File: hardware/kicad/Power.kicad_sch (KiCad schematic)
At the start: 53 parts, among them J1 USB_C_Receptacle_USB2.0_16P, Q1 FDN304PZ, SW1 SW_SPDT_321, U1 TPS61023DRLR, U2 MCP73871-2CC, U3 TLV74333PDBVR, U4 TLV74333PDBVR

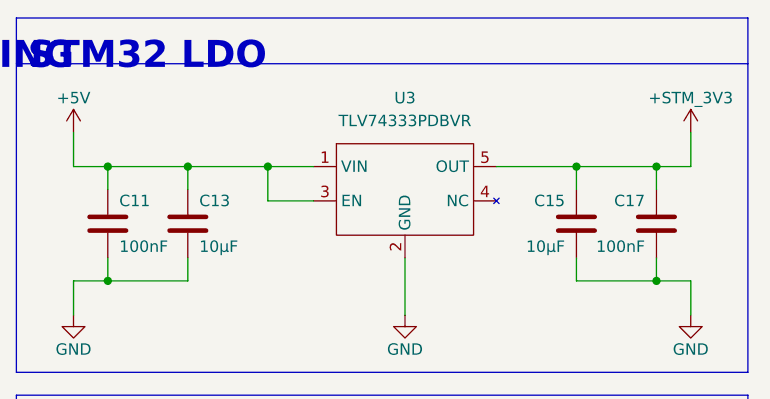
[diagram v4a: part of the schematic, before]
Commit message: completed schematics and started pcb
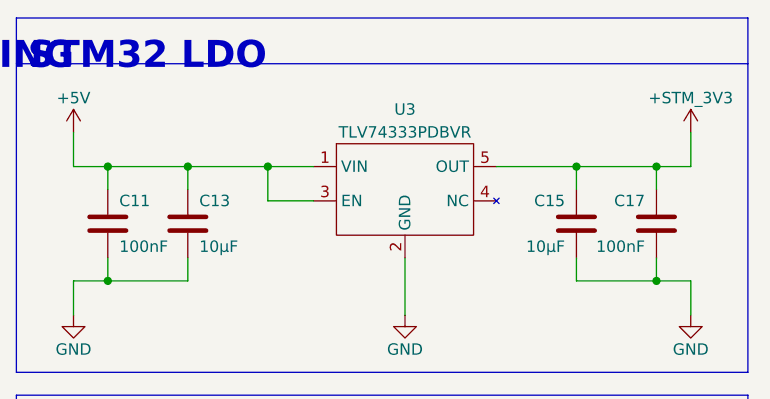
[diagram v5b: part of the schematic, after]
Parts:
- U2: footprint Package_DFN_QFN:QFN-20-1EP_4x4mm_P0.5mm_EP2.5x2.5mm -> Package_DFN_QFN:QFN-20-1EP_4x4mm_P0.5mm_EP2.5x2.5mm_ThermalVias
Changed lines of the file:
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@@
+	)
+	(symbol
+		(lib_id "TLV74333PDBVR:TLV74333PDBVR")
+		(at 245.11 33.02 0)
+		(unit 1)
+		(body_style 1)
+		(exclude_from_sim no)
+		(in_bom yes)
+		(on_board yes)
+		(in_pos_files yes)
+		(dnp no)
+		(property "Reference" "U3"
+			(at 245.11 24.13 0)
+			(show_name no)
+			(do_not_autoplace no)
+			(effects
+				(font
+					(size 1.27 1.27)
+				)
+			)
+		)
+		(property "Value" "TLV74333PDBVR"
+			(at 245.11 26.67 0)
+			(show_name no)
+			(do_not_autoplace no)
+			(effects
+				(font
+					(size 1.27 1.27)
+				)
+			)
+		)
+		(property "Footprint" "Package_TO_SOT_SMD:SOT-23-5_HandSoldering"
+			(at 246.38 52.07 0)
+			(hide yes)
+			(show_name no)
+			(do_not_autoplace no)
+			(effects
+				(font
+					(size 1.27 1.27)
+				)
+			)
+		)
+		(property "Datasheet" ""
+			(at 245.11 33.02 0)
+			(hide yes)
+			(show_name no)
+			(do_not_autoplace no)
+			(effects
+				(font
+					(size 1.27 1.27)
+				)
+			)
+		)
+		(property "Description" ""
+			(at 245.11 33.02 0)
+			(hide yes)
+			(show_name no)
+			(do_not_autoplace no)
+			(effects
+				(font
+					(size 1.27 1.27)
+				)
+			)
+		)
+		(pin "2"
+		)
+		(pin "5"
+		)
+		(pin "4"
+		)
+		(pin "1"
+		)
+		(pin "3"
+		)
+		(instances
+			(project "crypto_node"
+				(path "/6c72b0cb-17b9-42a6-811c-297d0c354af3/0878dbd6-f23a-45b7-803f-70f55a38d748"
+					(reference "U3")
+					(unit 1)
+				)
+			)
+		)
 	)
 	(symbol
@@
 			)
 		)
-		(property "Footprint" "Package_DFN_QFN:QFN-20-1EP_4x4mm_P0.5mm_EP2.5x2.5mm"
+		(property "Footprint" "Package_DFN_QFN:QFN-20-1EP_4x4mm_P0.5mm_EP2.5x2.5mm_ThermalVias"
 			(at 134.62 119.38 0)
 			(hide yes)
@@
 					(unit 1)
 				)
-			)
-		)
-	)
-	(symbol
-		(lib_id "TLV74333PDBVR:TLV74333PDBVR")
-		(at 245.11 33.02 0)
-		(unit 1)
-		(body_style 1)
-		(exclude_from_sim no)
-		(in_bom yes)
-		(on_board yes)
-		(in_pos_files yes)
-		(dnp no)
-		(fields_autoplaced yes)
-		(property "Reference" "U3"
-			(at 245.11 22.86 0)
-			(show_name no)
-			(do_not_autoplace no)
-			(effects
-				(font
-					(size 1.27 1.27)
-				)
-			)
-		)
-		(property "Value" "TLV74333PDBVR"
-			(at 245.11 25.4 0)
-			(show_name no)
-			(do_not_autoplace no)
-			(effects
-				(font
-					(size 1.27 1.27)
-				)
-			)
-		)
-		(property "Footprint" "Package_TO_SOT_SMD:SOT-23-5_HandSoldering"
-			(at 246.38 52.07 0)
-			(hide yes)
-			(show_name no)
-			(do_not_autoplace no)
-			(effects
-				(font
-					(size 1.27 1.27)
-				)
-			)
-		)
-		(property "Datasheet" ""
-			(at 245.11 33.02 0)
-			(hide yes)
-			(show_name no)
-			(do_not_autoplace no)
-			(effects
-				(font
-					(size 1.27 1.27)
-				)
-			)
-		)
-		(property "Description" ""
-			(at 245.11 33.02 0)
-			(hide yes)
-			(show_name no)
-			(do_not_autoplace no)
-			(effects
-				(font
-					(size 1.27 1.27)
-				)
-			)
-		)
-		(pin "2"
-		)
-		(pin "5"
-		)
-		(pin "4"
-		)
-		(pin "1"
-		)
-		(pin "3"
-		)
-		(instances
-			(project "crypto_node"
-				(path "/6c72b0cb-17b9-42a6-811c-297d0c354af3/0878dbd6-f23a-45b7-803f-70f55a38d748"
-					(reference "U3")
-					(unit 1)
-				)

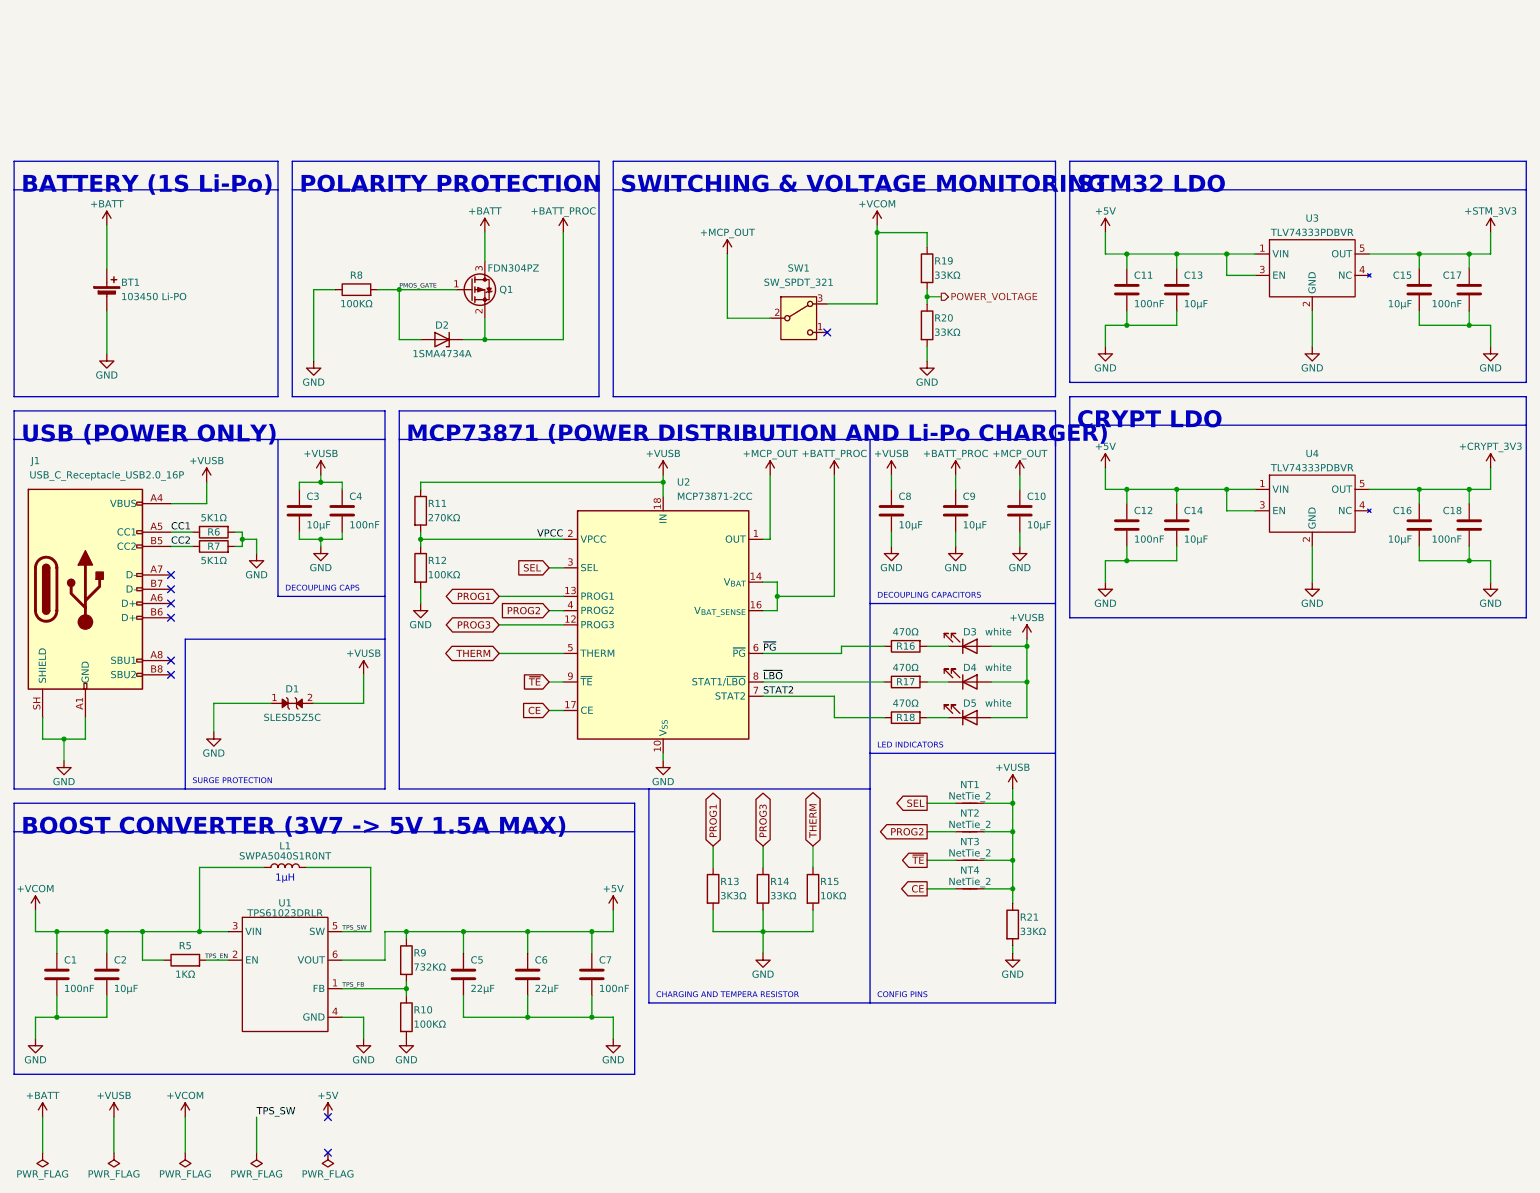
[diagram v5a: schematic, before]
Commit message: started PCB and changed power system
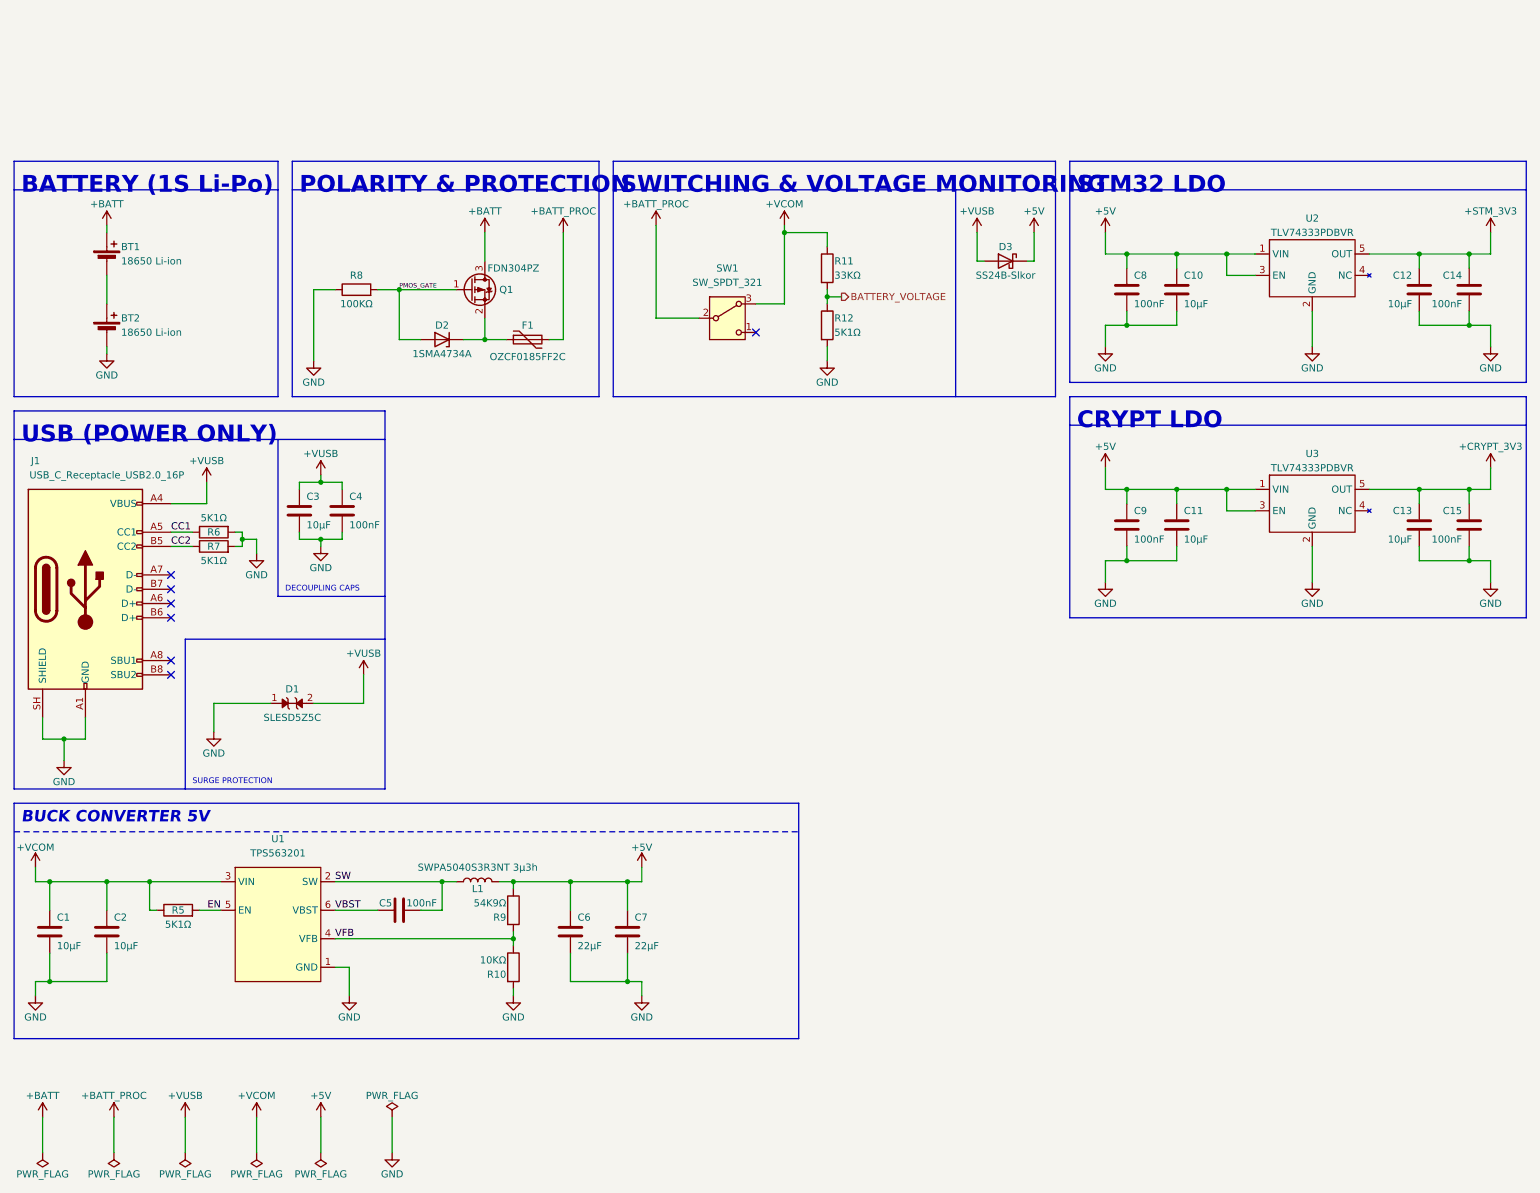
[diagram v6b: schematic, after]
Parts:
- removed C10, C8, C9: 10μF, Capacitor_SMD:C_1206_3216Metric_Pad1.33x1.80mm_HandSolder, symbol Device:C
- removed D3, D4, D5: white, LED_SMD:LED_0805_2012Metric_Pad1.15x1.40mm_HandSolder, symbol Device:LED
- removed NT1, NT2, NT3, NT4: NetTie_2, NetTie:NetTie-2_SMD_Pad0.5mm, symbol Device:NetTie_2
- removed R11: 270KΩ, Resistor_SMD:R_0805_2012Metric_Pad1.20x1.40mm_HandSolder, symbol Device:R
- removed R13: 3K3Ω, Resistor_SMD:R_0805_2012Metric_Pad1.20x1.40mm_HandSolder, symbol Device:R
- removed R14, R20, R21: 33KΩ, Resistor_SMD:R_0805_2012Metric_Pad1.20x1.40mm_HandSolder, symbol Device:R
- removed R15: 10KΩ, Resistor_SMD:R_0805_2012Metric_Pad1.20x1.40mm_HandSolder, symbol Device:R
- removed R16, R17, R18: 470Ω, Resistor_SMD:R_0805_2012Metric_Pad1.20x1.40mm_HandSolder, symbol Device:R
- removed U1: TPS61023DRLR, Package_TO_SOT_SMD:SOT-563, symbol TPS61023DRLR:TPS61023DRLR
- removed U2: MCP73871-2CC, Package_DFN_QFN:QFN-20-1EP_4x4mm_P0.5mm_EP2.5x2.5mm_ThermalVias, symbol Battery_Management:MCP73871-2CC
- added BT2: 18650 Li-ion, Battery:BatteryHolder_Keystone_1042_1x18650, symbol Device:Battery_Cell
- added D3: SS24B-Slkor, Diode_SMD:D_SMA, symbol Device:D_Schottky
- added F1: OZCF0185FF2C, Fuse:Fuse_2920_7451Metric_Pad2.10x5.45mm_HandSolder, symbol Device:Polyfuse
- added U1: TPS563201, Package_TO_SOT_SMD:SOT-23-6, symbol TPS563201:TPS563201
- BT1: value 103450 Li-PO -> 18650 Li-ion; footprint Connector_JST:JST_PH_B2B-PH-K_1x02_P2.00mm_Vertical -> Battery:BatteryHolder_Keystone_1042_1x18650
- C1: value 100nF -> 10μF; footprint Capacitor_SMD:C_0603_1608Metric_Pad1.08x0.95mm_HandSolder -> Capacitor_SMD:C_1206_3216Metric_Pad1.33x1.80mm_HandSolder
- C5: value 22μF -> 100nF; footprint Capacitor_SMD:C_1210_3225Metric_Pad1.33x2.70mm_HandSolder -> Capacitor_SMD:C_0603_1608Metric_Pad1.08x0.95mm_HandSolder
- C7: value 100nF -> 22μF; footprint Capacitor_SMD:C_0603_1608Metric_Pad1.08x0.95mm_HandSolder -> Capacitor_SMD:C_1210_3225Metric_Pad1.33x2.70mm_HandSolder
- L1: value SWPA5040S1R0NT -> SWPA5040S3R3NT 3μ3h
- R10: value 100KΩ -> 10KΩ
- R12: value 100KΩ -> 5K1Ω
- R5: value 1KΩ -> 5K1Ω
- R9: value 732KΩ -> 54K9Ω
- renumbered C13 to C10, C14 to C11, C15 to C12, C16 to C13, C17 to C14, C18 to C15, C11 to C8, C12 to C9, R19 to R11, U3 to U2, U4 to U3
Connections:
- net +MCP_OUT is gone; now on net +BATT_PROC: SW1.2 (B)
- net TPS_SW is gone; now on net +5V: L1.2
- net VPCC is gone; now on net BATTERY_VOLTAGE: R12.1
- net +5V: now also D3.1 (K); no longer C5.1
- net +BATT_PROC: now also F1.2; no longer D2.1 (K), Q1.2 (S)
- net +VCOM: now also U1.3 (VIN); no longer L1.1
- net +VUSB: now also D3.2 (A)
- net GND: now also BT2.2 (-), U1.1 (GND); no longer BT1.2 (-), C5.2
- net POWER_VOLTAGE renamed BATTERY_VOLTAGE
- net TPS_EN renamed EN
- net EN: now also U1.5 (EN)
- net TPS_FB renamed VFB
- net VFB: now also U1.4 (VFB)
- new net: BT1.2 (-), BT2.1 (+)
- new net: D2.1 (K), F1.1, Q1.2 (S)
- new net SW: C5.2, L1.1, U1.2 (SW)
- new net VBST: C5.1, U1.6 (VBST)
- no-connect marks 9 -> 7
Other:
- note added: "BUCK CONVERTER 5V"
- note added: "POLARITY & PROTECTION"
- note removed: "1μH"
- note removed: "BOOST CONVERTER (3V7 -> 5V 1.5A MAX)"
- note removed: "CHARGING AND TEMPERA RESISTOR"
- note removed: "CONFIG PINS"
- note removed: "DECOUPLING CAPACITORS"
- note removed: "LED INDICATORS"
- note removed: "MCP73871 (POWER DISTRIBUTION AND Li-Po CHARGER)"
- note removed: "POLARITY PROTECTION"
- moved on the sheet: BT1, R11, SW1

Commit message: finished pcb
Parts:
- renumbered J1 to J2
